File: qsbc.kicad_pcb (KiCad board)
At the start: 8 copper layers, 80 x 80 mm, 380 parts, among them J1 USB_C_Receptacle_USB2.0, J2 USB_C_Receptacle_USB2.0, J3 USB_C_Receptacle_USB2.0, J4 USB_C_Receptacle_USB2.0, J5 ARJM11D7-502-AB-EW2, J6 Micro_SD_Card_Det1, J7 Conn_ARM_JTAG_SWD_10, J8 1-2199230-6, SW1 SW_Push, SW2 SW_DIP_x02, U1 MIMX8MM6DVTLZAA, U10 TUSB320LAI, U11 D5V0H1B2LP, U12 D5V0H1B2LP, U13 TPD4EUSB30, U14 TPD4EUSB30, U15 74LVC1G07, U16 74LVC1G07, U17 D5V0H1B2LP, U18 CH343P, U19 TPD4EUSB30, U2 MT40A1G16KD-062E, U20 INA231, U21 D5V0H1B2LP, U22 TS3USB221E, U23 TPD4EUSB30, U24 RTL8211FD, U25 TPD4EUSB30, U26 TPD4EUSB30, U27 TPD4EUSB30, U28 D5V0H1B2LP, U29 W25Q32JWZP, U3 BD71847MWV, U30 SiP32431DR3, U31 TPD4EUSB30, U32 74LVC1G07, U33 74LVC1G07, U34 SI52112-B5-GM2, U35 74LVC1G07, U36 74LVC1G07, U4 NCP718BSN250T1G, U5 74LVC1G04, U6 74LVC1G04, U7 NX5P3363, U8 TUSB320LAI, U9 NX5P3363, Y1 Crystal, Y2 25MHz, Y3 24Mhz, Y4 25MHz

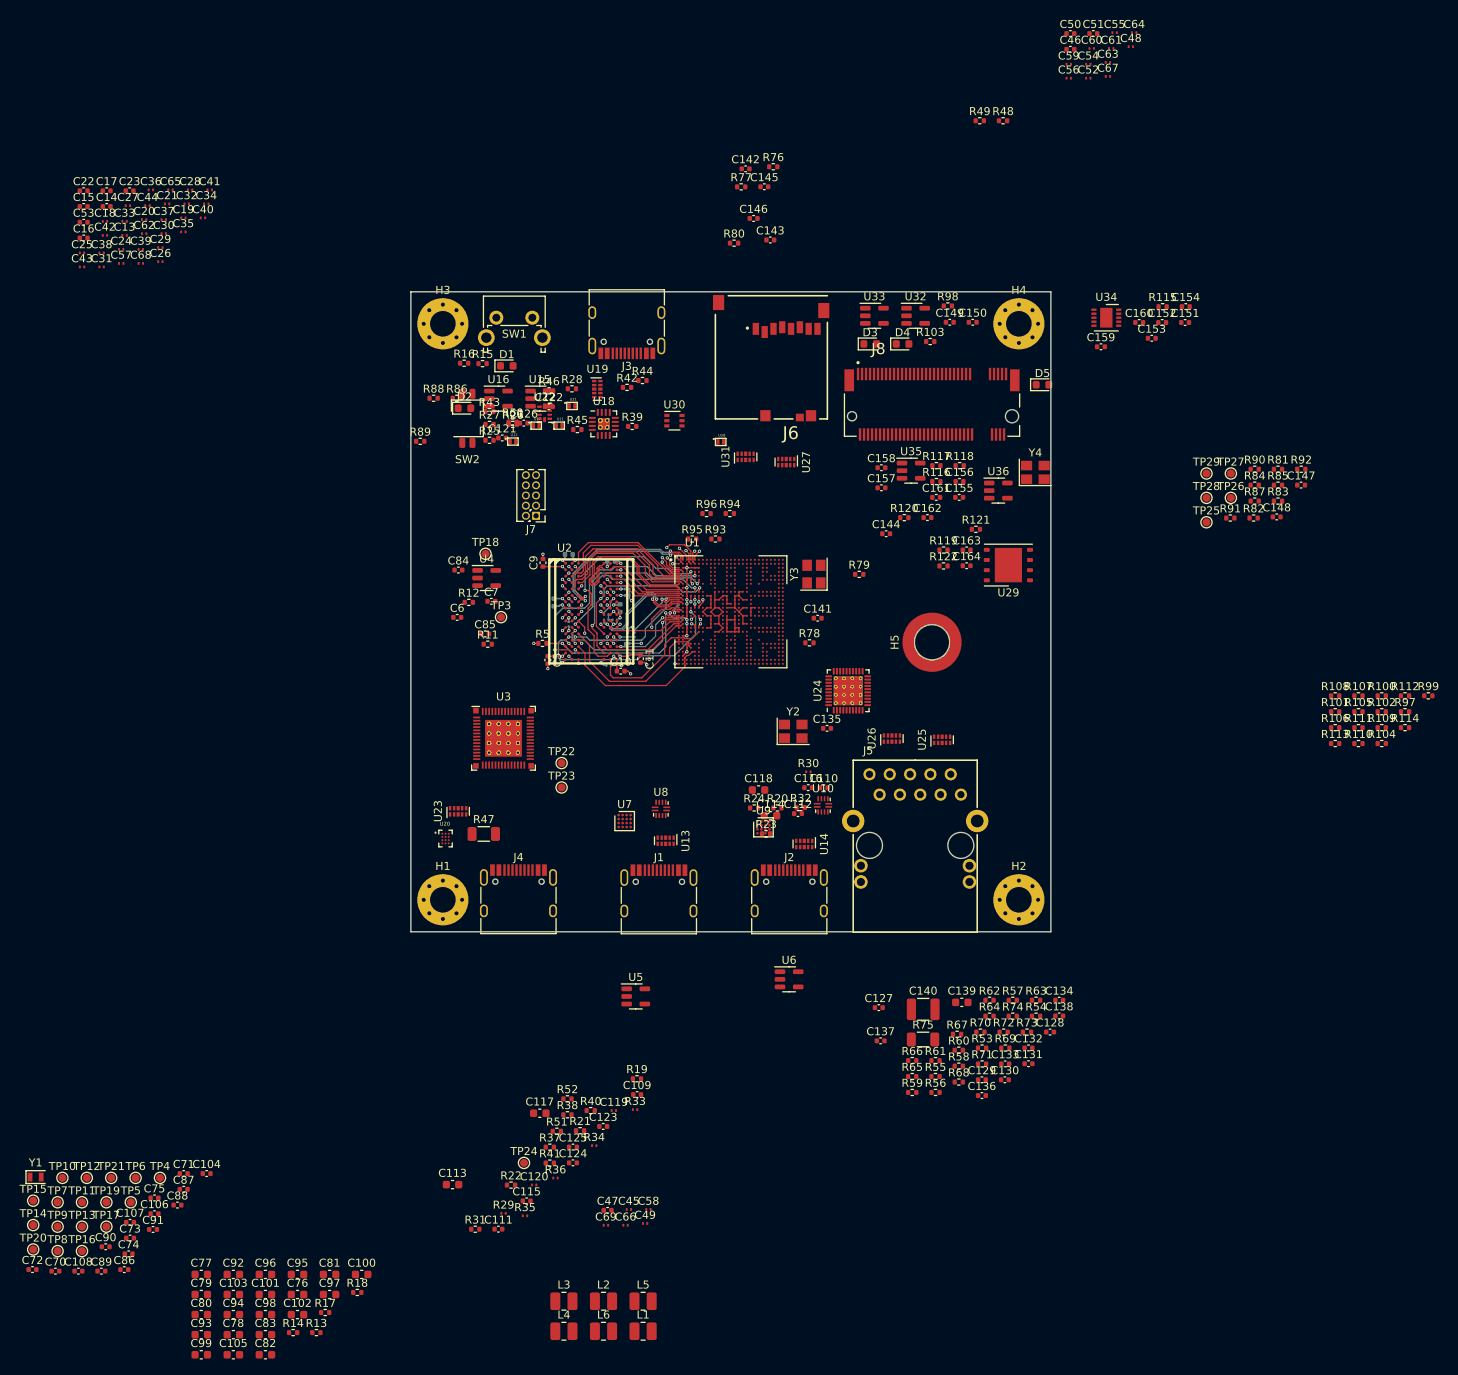
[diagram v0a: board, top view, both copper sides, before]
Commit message: v2 of ddr flytimes tool, lots of routing work, sch fixes
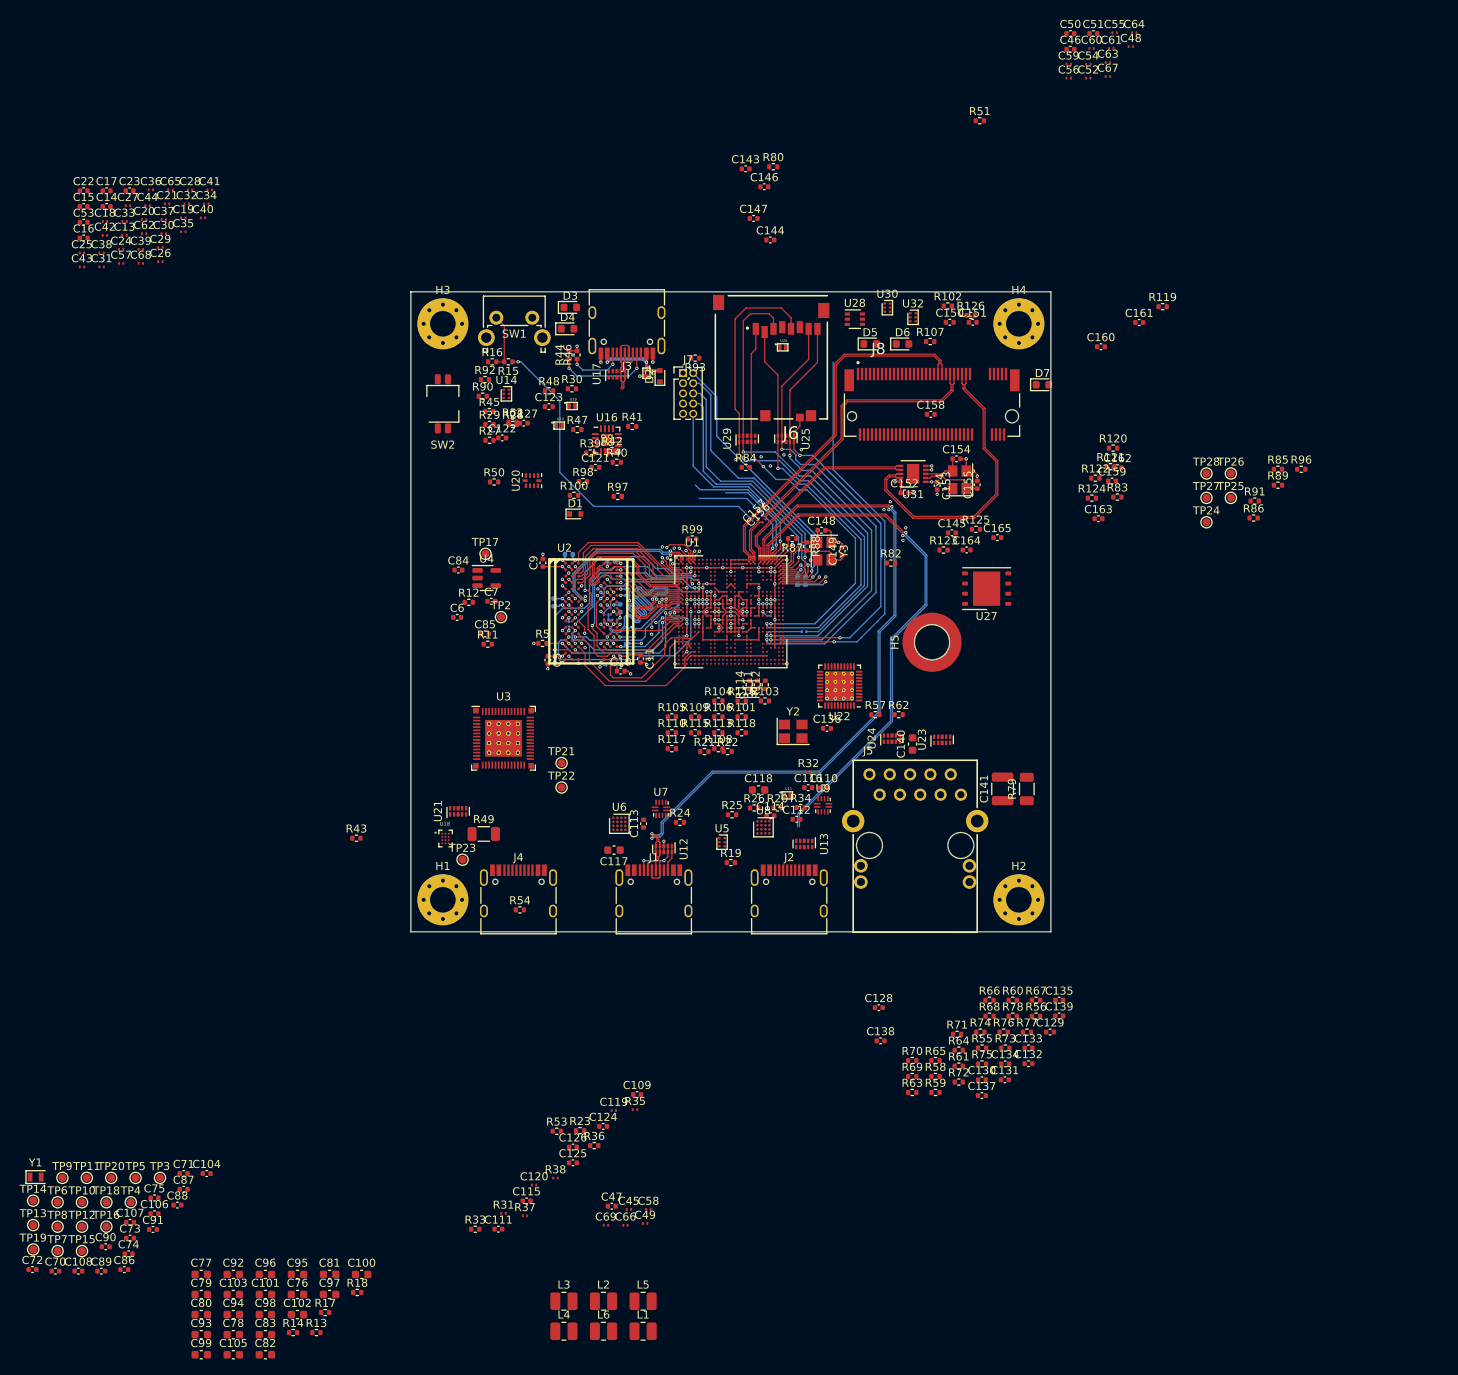
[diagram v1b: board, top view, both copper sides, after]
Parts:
- removed the U15 at (124.0, 72.3)
- removed the U16 at (118.9, 72.3)
- removed U33, U35, U36: 74LVC1G07, Package_TO_SOT_SMD:SOT-23-5
- removed the U6 at (155.2, 144.9)
- added C121: 1uF, Capacitor_SMD:C_0402_1005Metric, F.Cu at (131.0, 80.9)
- added D1: D_Schottky, Diode_SMD:D_SOD-523, F.Cu at (128.5, 86.7)
- added D2: D_Schottky, Diode_SMD:D_SOD-523, F.Cu at (139.1, 69.5)
- added R21: 10K, Resistor_SMD:R_0402_1005Metric, F.Cu at (144.6, 116.4)
- added R22: 10K, Resistor_SMD:R_0402_1005Metric, F.Cu at (147.5, 116.4)
- added R57: 4.7K, Resistor_SMD:R_0402_1005Metric, F.Cu at (166.0, 111.8)
- added R62: 4.7K, Resistor_SMD:R_0402_1005Metric, F.Cu at (168.9, 111.8)
- added U14: 74LVC2G07, Package_TO_SOT_SMD:SOT-886, F.Cu at (119.9, 71.7)
- added U30: 74LVC2G07, Package_TO_SOT_SMD:SOT-886, F.Cu at (167.5, 60.9)
- C113, C114: footprint Capacitor_SMD:C_0603_1608Metric -> Capacitor_SMD:C_0402_1005Metric
- C142: renamed from C141; footprint Capacitor_SMD:C_0402_1005Metric -> qsbc:C_0201_0603Metric; moved to B.Cu
- C156: renamed from C155; footprint Capacitor_SMD:C_0402_1005Metric -> qsbc:C_0201_0603Metric
- C157: renamed from C156; footprint Capacitor_SMD:C_0402_1005Metric -> qsbc:C_0201_0603Metric
- R36: renamed from R34; footprint qsbc:R_0201_0603Metric -> Resistor_SMD:R_0402_1005Metric
- R81: renamed from R78; footprint Resistor_SMD:R_0402_1005Metric -> qsbc:R_0201_0603Metric; moved to B.Cu
- R94: renamed from R90; moved to B.Cu
- R95: renamed from R91; moved to B.Cu
- U32: value 74LVC1G07 -> 74LVC2G07; footprint Package_TO_SOT_SMD:SOT-23-5 -> Package_TO_SOT_SMD:SOT-886
- U5: value 74LVC1G04 -> 74LVC2G04; footprint Package_TO_SOT_SMD:SOT-23-5 -> Package_TO_SOT_SMD:SOT-886
- moved R39 86.9 mm to (130.4, 79.1)
- moved R101 82.9 mm to (149.3, 112.1)
- moved R103 82.9 mm to (152.2, 110.1)
- moved R104 82.9 mm to (146.4, 110.1)
- moved R106 82.9 mm to (146.4, 112.1)
- moved R108 82.9 mm to (146.4, 116.0)
- moved R113 82.9 mm to (146.4, 114.0)
- moved R116 82.9 mm to (149.3, 110.1)
- moved R118 82.9 mm to (149.3, 114.0)
- moved R105 82.9 mm to (140.6, 112.1)
- moved R109 82.9 mm to (143.5, 112.1)
- moved R110 82.9 mm to (140.6, 114.0)
- moved R115 82.9 mm to (143.5, 114.0)
- moved R117 82.9 mm to (140.6, 116.0)
- moved R42 82.5 mm to (133.1, 78.8)
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- renumbered C121 to C122, C122 to C123, C123 to C124, C124 to C125, C125 to C126, C126 to C127, C127 to C128, C128 to C129, C129 to C130, C130 to C131, C131 to C132, C132 to C133, C133 to C134, C134 to C135, C135 to C136, C136 to C137, C137 to C138, C138 to C139, C139 to C140, C140 to C141, C142 to C143, C143 to C144, C144 to C145, C145 to C146, C146 to C147, C147 to C148, C148 to C149, C149 to C150, C150 to C151, C151 to C152, C152 to C153, C153 to C154, C154 to C155, C157 to C158, C158 to C159, C159 to C160, C160 to C161, C161 to C162, C162 to C163, C163 to C164, C164 to C165, D1 to D3, D2 to D4, D3 to D5, D4 to D6, D5 to D7, R96 to R100, R97 to R101, R98 to R102, R99 to R103, R100 to R104, R101 to R105, R102 to R106, R103 to R107, R104 to R108, R105 to R109, R106 to R110, R107 to R111, R108 to R112, R109 to R113, R110 to R114, R111 to R115, R112 to R116, R113 to R117, R114 to R118, R115 to R119, R116 to R120, R117 to R121, R118 to R122, R119 to R123, R120 to R124, R121 to R125, R122 to R126, R21 to R23, R22 to R24, R23 to R25, R24 to R26, R25 to R27, R26 to R28, R27 to R29, R28 to R30, R29 to R31, R30 to R32, R31 to R33, R32 to R34, R33 to R35, R35 to R37, R36 to R38, R37 to R39, R38 to R40, R39 to R41, R40 to R42, R41 to R43, R42 to R44, R43 to R45, R44 to R46, R45 to R47, R46 to R48, R47 to R49, R48 to R50, R49 to R51, R50 to R52, R51 to R53, R52 to R54, R53 to R55, R54 to R56, R55 to R58, R56 to R59, R57 to R60, R58 to R61, R59 to R63, R60 to R64, R61 to R65, R62 to R66, R63 to R67, R64 to R68, R65 to R69, R66 to R70, R67 to R71, R68 to R72, R69 to R73, R70 to R74, R71 to R75, R72 to R76, R73 to R77, R74 to R78, R75 to R79, R76 to R80, R79 to R82, R77 to R83, R80 to R84, R81 to R85, R82 to R86, R83 to R87, R84 to R88, R85 to R89, R86 to R90, R87 to R91, R88 to R92, R89 to R93, R92 to R96, R93 to R97, R94 to R98, R95 to R99, TP2 to TP1, TP11 to TP10, TP12 to TP11, TP13 to TP12, TP14 to TP13, TP15 to TP14, TP16 to TP15, TP17 to TP16, TP18 to TP17, TP19 to TP18, TP20 to TP19, TP3 to TP2, TP21 to TP20, TP22 to TP21, TP23 to TP22, TP24 to TP23, TP25 to TP24, TP26 to TP25, TP27 to TP26, TP28 to TP27, TP29 to TP28, TP4 to TP3, TP5 to TP4, TP6 to TP5, TP7 to TP6, TP8 to TP7, TP9 to TP8, TP10 to TP9, U11 to U10, U12 to U11, U13 to U12, U14 to U13, U17 to U15, U18 to U16, U19 to U17, U20 to U18, U21 to U19, U22 to U20, U23 to U21, U24 to U22, U25 to U23, U26 to U24, U27 to U25, U28 to U26, U29 to U27, U30 to U28, U31 to U29, U34 to U31, U7 to U6, U8 to U7, U9 to U8, U10 to U9
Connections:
- net Net-(C147-Pad1) renamed /Misc/24M_XTALI
- net Net-(C148-Pad1) renamed /Misc/24M_XTALO
- net Net-(R83-Pad2) renamed /Misc/RTC_XTALO
- C125 pad 1: VDD_3.3V -> /USB/CH343_V3
- D5 pad 1: Net-(D3-Pad1) (its old number) -> Net-(D5-Pad1)
- R29 pad 1: Net-(R27-Pad1) -> Net-(R29-Pad1)
- R30 pad 1: Net-(R28-Pad1) -> Net-(R30-Pad1)
- U12 pad 1: /USB/USB1_CC1 -> /USB/USB1_CC2
- U12 pad 10: /USB/USB1_CC1 -> /USB/USB1_CC2
- U12 pad 2: /USB/USB1_CC2 -> /USB/USB1_CC1
- U12 pad 4: /USB/USB1_DN -> /USB/USB1_DP
- U12 pad 5: /USB/USB1_DP -> /USB/USB1_DN
- U12 pad 6: /USB/USB1_DP -> /USB/USB1_DN
- U12 pad 7: /USB/USB1_DN -> /USB/USB1_DP
- U12 pad 9: /USB/USB1_CC2 -> /USB/USB1_CC1
- U13 pad 1: /USB/USB2_CC1 -> /USB/USB2_CC2
- U13 pad 10: /USB/USB2_CC1 -> /USB/USB2_CC2
- U13 pad 2: /USB/USB2_CC2 -> /USB/USB2_CC1
- U13 pad 4: /USB/USB2_DN -> /USB/USB2_DP
- U13 pad 5: /USB/USB2_DP -> /USB/USB2_DN
- U13 pad 6: /USB/USB2_DP -> /USB/USB2_DN
- U13 pad 7: /USB/USB2_DN -> /USB/USB2_DP
- U13 pad 9: /USB/USB2_CC2 -> /USB/USB2_CC1
- U16 pad 3: VDD_3.3V -> /USB/VDD_UART_5V
- U16 pad 6: VDD_3.3V -> /USB/CH343_V3
- U16 pad 9: VDD_3.3V -> /USB/VDD_UART_5V
- U25 pad 1: /Storage/SD2_DATA1 -> /Storage/~{SD2_CD}
- U25 pad 10: /Storage/SD2_DATA1 -> /Storage/~{SD2_CD}
- U25 pad 2: /Storage/SD2_DATA0 -> /Storage/SD2_DATA1
- U25 pad 4: /Storage/SD2_DATA3 -> /Storage/SD2_DATA0
- U25 pad 5: /Storage/SD2_DATA2 -> /Storage/SD2_DATA3
- U25 pad 6: /Storage/SD2_DATA2 -> /Storage/SD2_DATA3
- U25 pad 7: /Storage/SD2_DATA3 -> /Storage/SD2_DATA0
- U25 pad 9: /Storage/SD2_DATA0 -> /Storage/SD2_DATA1
- U29 pad 1: /Storage/SD2_CMD -> /Storage/SD2_CLK
- U29 pad 10: /Storage/SD2_CMD -> /Storage/SD2_CLK
- U29 pad 2: /Storage/SD2_CLK -> /Storage/SD2_CMD
- U29 pad 4: /Storage/~{SD2_CD} -> /Storage/SD2_DATA2
- U29 pad 7: /Storage/~{SD2_CD} -> /Storage/SD2_DATA2
- U29 pad 9: /Storage/SD2_CLK -> /Storage/SD2_CMD
- U32 pad 1: (no net) -> /PCIe/~{M2_RESET}
- U32 pad 2: /Peripherals/LED0 -> GND
- U32 pad 3: GND -> /PCIe/~{M2_WAKE_3.3V}
- U32 pad 4: Net-(D3-Pad1) (its old number) -> /PCIe/~{M2_WAKE}
- U5 pad 1: (no net) -> /USB/USB1_ID
- U5 pad 2: /USB/USB1_ID -> GND
- U5 pad 3: GND -> /USB/USB2_ID
- U5 pad 4: Net-(R27-Pad1) -> Net-(R30-Pad1)
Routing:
- net GND: track 40.6 -> 133.9 mm, vias 35 -> 96
- net /USB/USB1_DP: track 0.00 -> 90.8 mm, vias 0 -> 2
- net /USB/USB1_DN: track 0.00 -> 90.1 mm, vias 0 -> 2
- net /USB/USB2_DN: track 0.00 -> 66.2 mm, vias 0 -> 1
- net /USB/USB2_DP: track 0.00 -> 66.1 mm, vias 0 -> 1
- net /Storage/SD2_CMD: track 0.00 -> 63.6 mm, vias 0 -> 2
- net /Storage/SD2_CLK: track 0.00 -> 62.2 mm, vias 0 -> 1
- net /Misc/ONOFF: track 0.00 -> 61.1 mm, vias 0 -> 2
- net /Storage/SD2_DATA0: track 0.00 -> 58.0 mm, vias 0 -> 2
- net /Storage/SD2_DATA1: track 0.00 -> 54.7 mm, vias 0 -> 2
- net /Storage/SD2_DATA3: track 0.00 -> 52.3 mm, vias 0 -> 2
- net /Storage/SD2_DATA2: track 0.00 -> 52.1 mm, vias 0 -> 2
- net /Storage/~{SD2_RESET}: track 0.00 -> 49.0 mm, vias 0 -> 1
- net /PCIe/PCIE_RX_P: track 0.00 -> 46.0 mm
- net /PCIe/PCIE_RX_N: track 0.00 -> 44.6 mm
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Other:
- rule pad_to_mask_clearance: 0.05 -> 0.03

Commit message: more routing work, prepare to change to x32 lpddr4
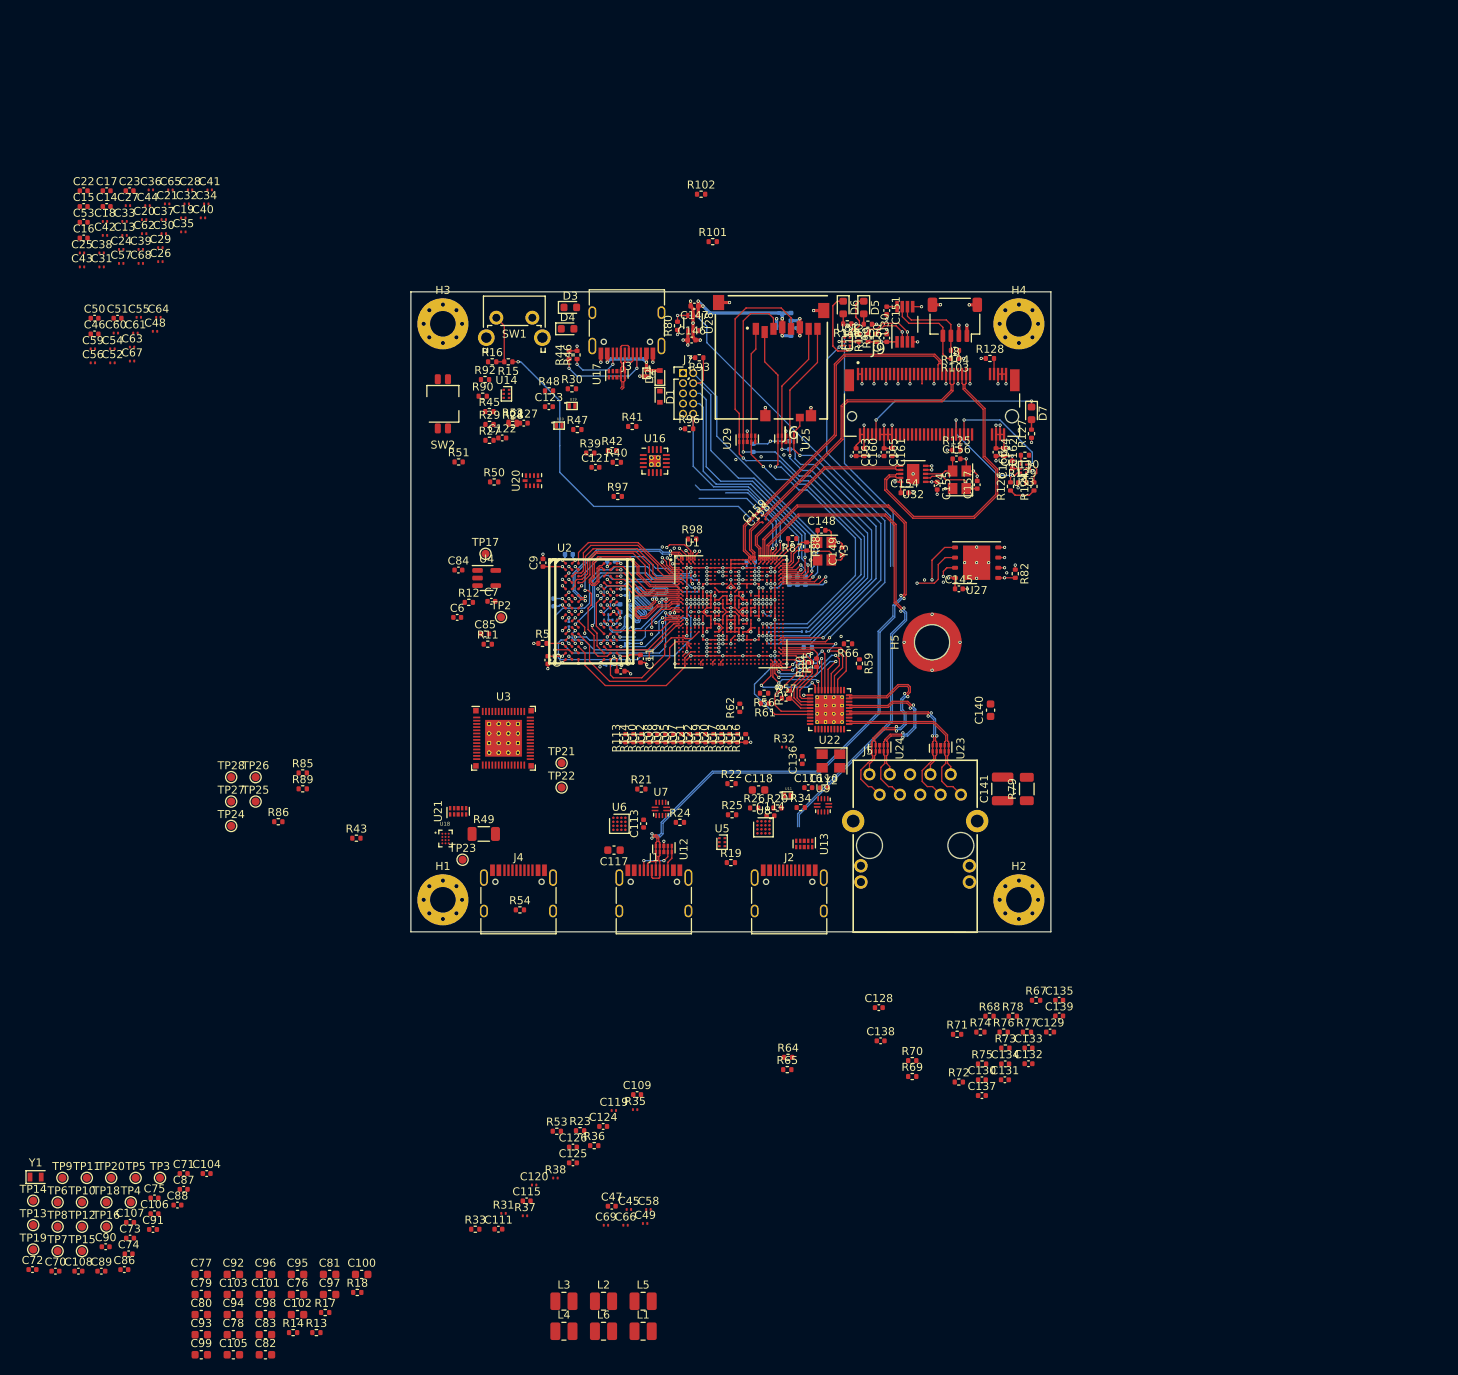
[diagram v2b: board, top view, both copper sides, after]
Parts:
- removed C112: 0.1uF, Capacitor_SMD:C_0402_1005Metric
- removed the C165 at (181.2, 89.7)
- added C150: 0.1uF, Capacitor_SMD:C_0402_1005Metric, F.Cu at (167.4, 64.7)
- added J8: Conn_01x04_MountingPin, Connector_JST:JST_SH_SM04B-SRSS-TB_1x04-1MP_P1.00mm_Horizontal, F.Cu at (175.9, 62.4)
- added R101: 4.7K, Resistor_SMD:R_0402_1005Metric, F.Cu at (145.7, 52.7)
- added R102: 4.7K, Resistor_SMD:R_0402_1005Metric, F.Cu at (144.2, 46.7)
- added R103: 4.7K, Resistor_SMD:R_0402_1005Metric, F.Cu at (175.9, 67.3)
- added R104: 4.7K, Resistor_SMD:R_0402_1005Metric, F.Cu at (175.9, 66.3)
- added U30: TCA9803, Package_SO:VSSOP-8_3.0x3.0mm_P0.65mm, F.Cu at (169.7, 63.0)
- C143, C144, R63, R83, R84, R91, U26: moved to B.Cu
- R123: renamed from R119; moved to B.Cu
- moved R85 127.7 mm to (94.4, 119.1)
- moved R89 127.7 mm to (94.4, 121.1)
- moved R86 127.7 mm to (91.4, 125.2)
- moved TP25 127.7 mm to (88.5, 122.7)
- moved TP26 127.7 mm to (88.5, 119.6)
- moved TP24 127.7 mm to (85.5, 125.7)
- moved TP27 127.7 mm to (85.5, 122.7)
- moved TP28 127.7 mm to (85.5, 119.6)
- moved C64 127.1 mm to (76.4, 62.1)
- moved C48 127.1 mm to (76.0, 63.9)
- moved C51 127.1 mm to (71.3, 62.2)
- moved C52 127.1 mm to (70.6, 67.8)
- moved C54 127.1 mm to (70.6, 66.1)
- moved C61 127.1 mm to (73.5, 64.1)
- moved C46 127.1 mm to (68.4, 64.2)
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- renumbered C150 to C152, C152 to C154, C153 to C155, C154 to C156, C155 to C157, C156 to C158, C157 to C159, C158 to C160, C159 to C161, C160 to C162, C161 to C163, C162 to C164, C163 to C165, C164 to C166, J8 to J9, R101 to R105, R102 to R106, R103 to R107, R104 to R108, R105 to R109, R106 to R110, R107 to R111, R108 to R112, R109 to R113, R110 to R114, R111 to R115, R112 to R116, R113 to R117, R114 to R118, R115 to R119, R116 to R120, R117 to R121, R118 to R122, R120 to R124, R121 to R125, R122 to R126, R123 to R127, R124 to R128, R125 to R129, R126 to R130, R99 to R98, R98 to R99, U30 to U31, U31 to U32, U32 to U33
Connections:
- C127 pad 1: VDD_3.3V -> /USB/CH343_V3
- C151 pad 1: VDD_1.8V -> VDD_3.3V
- R100 pad 2: /Peripherals/I2C4_SCL -> /Peripherals/I2C2_SDA
- R106 pad 1: /Peripherals/VDD_3.3V -> VDD_3.3V
- R111 pad 1: /Peripherals/VDD_3.3V -> VDD_3.3V
- R51 pad 1: VDD_3.3V -> /USB/CH343_V3
- R57 pad 2: /Ethernet/ENET_RD1 -> /Ethernet/ENET_RD0
- R58 pad 1: /Ethernet/ENET_RD1 -> /Ethernet/ENET_RD0
- R62 pad 2: /Ethernet/ENET_RD0 -> /Ethernet/ENET_RD1
- R63 pad 1: /Ethernet/ENET_RD0 -> /Ethernet/ENET_RD1
- R80 pad 1: /Storage/NVCC_SD2 -> /Power/NVCC_SD2
- R83 pad 1: /Storage/NVCC_SD2 -> /Power/NVCC_SD2
- R84 pad 1: /Storage/NVCC_SD2 -> /Power/NVCC_SD2
- R99 pad 2: /Peripherals/I2C4_SDA -> /Peripherals/I2C2_SCL
- U1 pad A6: unconnected-(U1-PadA6) -> /Peripherals/UART4_RTS
- U1 pad A8: /PCIe/~{M2_RESET} -> /Peripherals/UART4_CTS
- U1 pad D10: unconnected-(U1-PadD10) -> /Peripherals/I2C2_SCL
- U1 pad D9: unconnected-(U1-PadD9) -> /Peripherals/I2C2_SDA
- U1 pad E6: unconnected-(U1-PadE6) -> /PCIe/~{M2_RESET}
- U16 pad 1: GND -> VDD_1.8V
- U16 pad 17: (no net) -> GND
- U20 pad 10: VDD_3.3V -> /USB/CH343_V3
- U23 pad 1: /Ethernet/TRD0_P -> /Ethernet/TRD0_N
- U23 pad 10: /Ethernet/TRD0_P -> /Ethernet/TRD0_N
- U23 pad 2: /Ethernet/TRD0_N -> /Ethernet/TRD0_P
- U23 pad 4: /Ethernet/TRD1_P -> /Ethernet/TRD1_N
- U23 pad 5: /Ethernet/TRD1_N -> /Ethernet/TRD1_P
- U23 pad 6: /Ethernet/TRD1_N -> /Ethernet/TRD1_P
- U23 pad 7: /Ethernet/TRD1_P -> /Ethernet/TRD1_N
- U23 pad 9: /Ethernet/TRD0_N -> /Ethernet/TRD0_P
- U24 pad 1: /Ethernet/TRD2_P -> /Ethernet/TRD2_N
- U24 pad 10: /Ethernet/TRD2_P -> /Ethernet/TRD2_N
- U24 pad 2: /Ethernet/TRD2_N -> /Ethernet/TRD2_P
- U24 pad 4: /Ethernet/TRD3_P -> /Ethernet/TRD3_N
- U24 pad 5: /Ethernet/TRD3_N -> /Ethernet/TRD3_P
- U24 pad 6: /Ethernet/TRD3_N -> /Ethernet/TRD3_P
- U24 pad 7: /Ethernet/TRD3_P -> /Ethernet/TRD3_N
- U24 pad 9: /Ethernet/TRD2_N -> /Ethernet/TRD2_P
- U32 pad 11: (no net) -> GND
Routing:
- net GND: track 133.9 -> 193.7 mm, vias 96 -> 166
- net /Peripherals/I2C2_SDA: track 0.00 -> 55.8 mm, vias 0 -> 2
- net /Peripherals/I2C2_SCL: track 0.00 -> 55.3 mm, vias 0 -> 2
- net VDD_3.3V: track 3.55 -> 39.1 mm, vias 2 -> 19
- net /Peripherals/LED0: track 0.00 -> 33.5 mm, vias 0 -> 1
- net VDD_1.8V: track 4.91 -> 37.8 mm, vias 0 -> 15
- net /Peripherals/LED1: track 0.00 -> 32.3 mm, vias 0 -> 1
- net /Ethernet/TRD3_P: track 0.00 -> 27.2 mm, vias 0 -> 2
- net /Ethernet/TRD2_P: track 0.00 -> 24.0 mm, vias 0 -> 2
- net /Ethernet/TRD3_N: track 0.00 -> 23.5 mm, vias 0 -> 2
- net Net-(D7-Pad1): track 0.00 -> 23.0 mm, vias 0 -> 2
- net /Ethernet/TRD1_P: track 0.00 -> 22.6 mm, vias 0 -> 2
- net /Ethernet/TRD0_P: track 0.00 -> 21.9 mm
- net /Storage/VDD_SD2: track 0.00 -> 21.3 mm, vias 0 -> 4
- net /Ethernet/TRD2_N: track 0.00 -> 20.5 mm, vias 0 -> 2
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- added copper zone on In4.Cu, net VDD_1.8V
